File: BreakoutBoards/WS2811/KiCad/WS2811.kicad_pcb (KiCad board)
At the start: 2 copper layers, 22.2 x 12.1 mm, 7 parts, among them J1 Conn_01x08_Pin, U1 WS2811

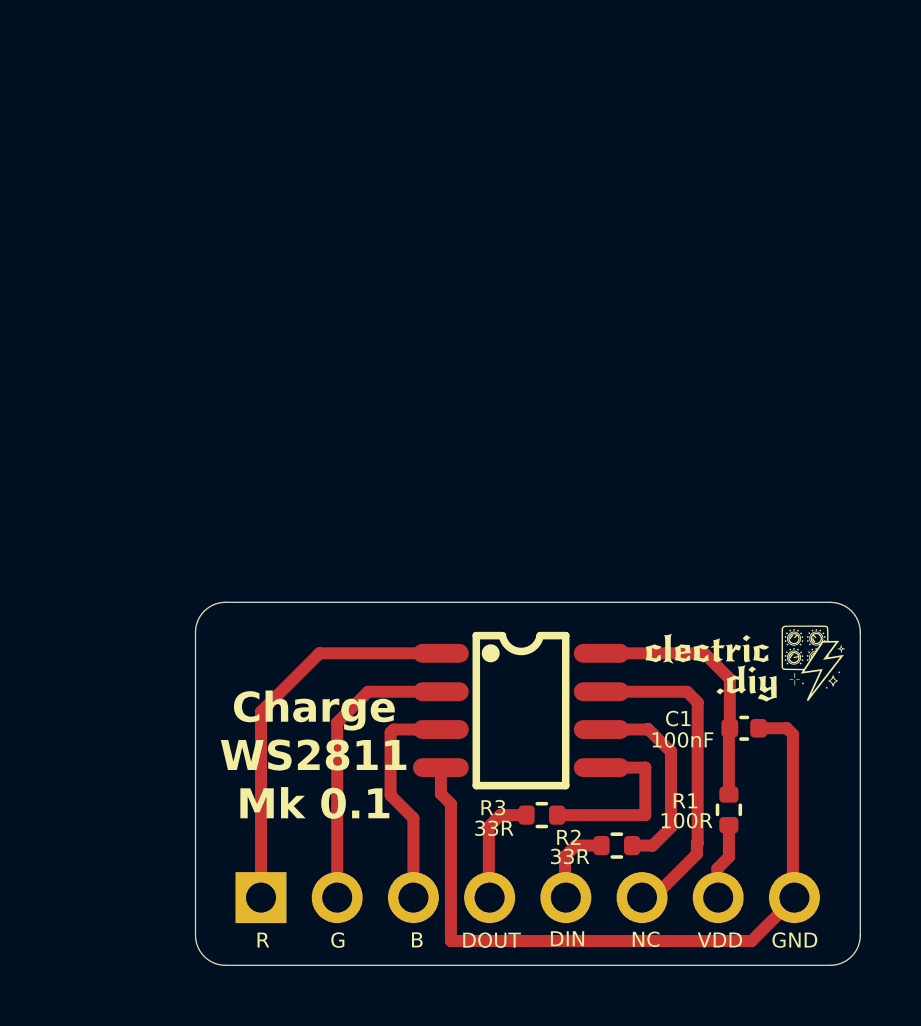
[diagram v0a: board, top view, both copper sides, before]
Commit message: ran DRC and resolved issues
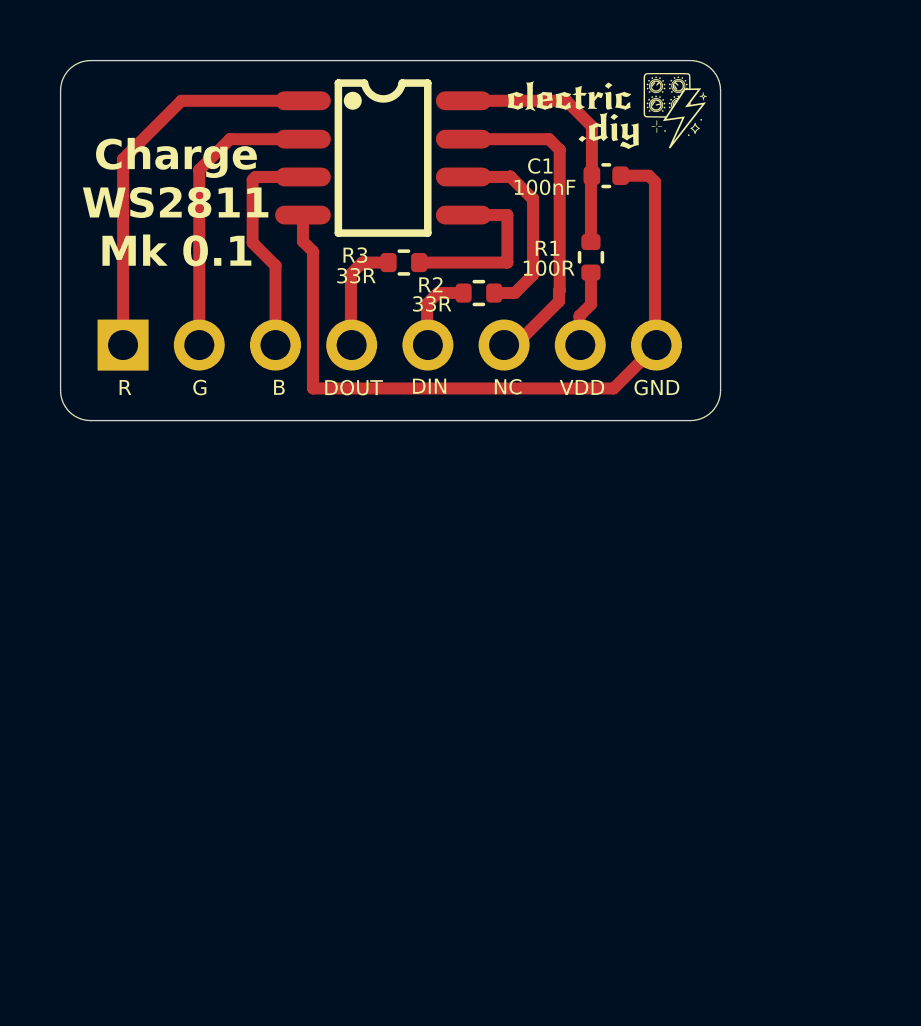
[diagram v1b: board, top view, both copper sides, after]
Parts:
- moved J1 19.0 mm to (93.6, 90.7)
- moved C1 19.0 mm to (109.7, 85.1)
- moved G*** 19.0 mm to (109.7, 82.9)
- moved R1 19.0 mm to (109.2, 87.8)
- moved R2 19.0 mm to (105.4, 89.0)
- moved R3 19.0 mm to (102.9, 88.0)
- moved U1 19.0 mm to (102.3, 84.5)
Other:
- board size 22.2 x 12.1 mm -> 22 x 12 mm

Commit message: updated to Mk1 and sent for manufacturing
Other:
- board text added: "Charge WS2811 Mk1"
- board text removed: "Charge WS2811 Mk 0.1"
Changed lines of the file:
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@@
 		(title "Charge WS2811")
 		(date "2026-02-20")
-		(rev "Mk 0.1")
+		(rev "Mk1")
 		(company "clectric.diy")
 		(comment 1 "Copyright © 2026 clectric.diy Licensed under CERN-OHL-W v2")
@@
 			(fill no)
 			(layer "F.Fab")
-		)
-		(fp_text user "${REFERENCE}"
-			(at 0 0 0)
-			(layer "F.Fab")
-			(effects
-				(font
-					(size 0.5 0.5)
-					(thickness 0.0625)
-				)
-			)
 		)
 		(pad "1" smd roundrect
@@
 			(layer "F.Fab")
 		)
-		(fp_text user "${REFERENCE}"
-			(at 0 0 0)
-			(layer "F.Fab")
-			(effects
-				(font
-					(size 0.5 0.5)
-					(thickness 0.0625)
-				)
-			)
-		)
 		(pad "1" smd roundrect
 			(at -0.51 0)
@@
 			(fill no)
 			(layer "F.Fab")
-		)
-		(fp_text user "${REFERENCE}"
-			(at 0 0 90)
-			(layer "F.Fab")
-			(effects
-				(font
-					(size 0.5 0.5)
-					(thickness 0.0625)
-				)
-			)
 		)
 		(pad "1" smd roundrect
@@
 		)
 	)
-	(gr_text "Charge\nWS2811\nMk 0.1"
+	(gr_text "Charge\nWS2811\nMk1"
 		(at 95.354 88.210798 0)
 		(layer "F.SilkS")
